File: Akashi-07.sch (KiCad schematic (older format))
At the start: 10 parts, among them U1 Si5351A-B-GT, U2 74HC74, U3 TS5A23157DGSR, U4 AD8032ANZ, X1 SG-615

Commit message: Update the switch symbol
Singal flow is natural now.
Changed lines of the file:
@@
 $EndDescr
-$Comp
-L TS5A23157:TS5A23157DGSR U3
-U 1 1 5F07B13A
-P 8150 1850
-F 0 "U3" H 8950 2337 60  0000 C CNN
-F 1 "TS5A23157DGSR" H 8950 2231 60  0000 C CNN
-F 2 "DGS10" H 8950 2190 60  0001 C CNN
-F 3 "" H 8150 1850 60  0000 C CNN
-	1    8150 1850
-	-1   0    0    -1
-$EndComp
 $Comp
 L Oscillator:Si5351A-B-GT U1
@@
 Text Notes 7050 2950 0    50   ~ 0
 Quadrature Switch
+$Comp
+L TS5A23157:TS5A23157DGSR U3
+U 1 1 5F0916DB
+P 6700 1350
+F 0 "U3" H 7500 1837 60  0000 C CNN
+F 1 "TS5A23157DGSR" H 7500 1731 60  0000 C CNN
+F 2 "DGS10" H 7500 1690 60  0001 C CNN
+F 3 "" H 6700 1350 60  0000 C CNN
+	1    6700 1350
+	1    0    0    -1
+$EndComp
 $EndSCHEMATC

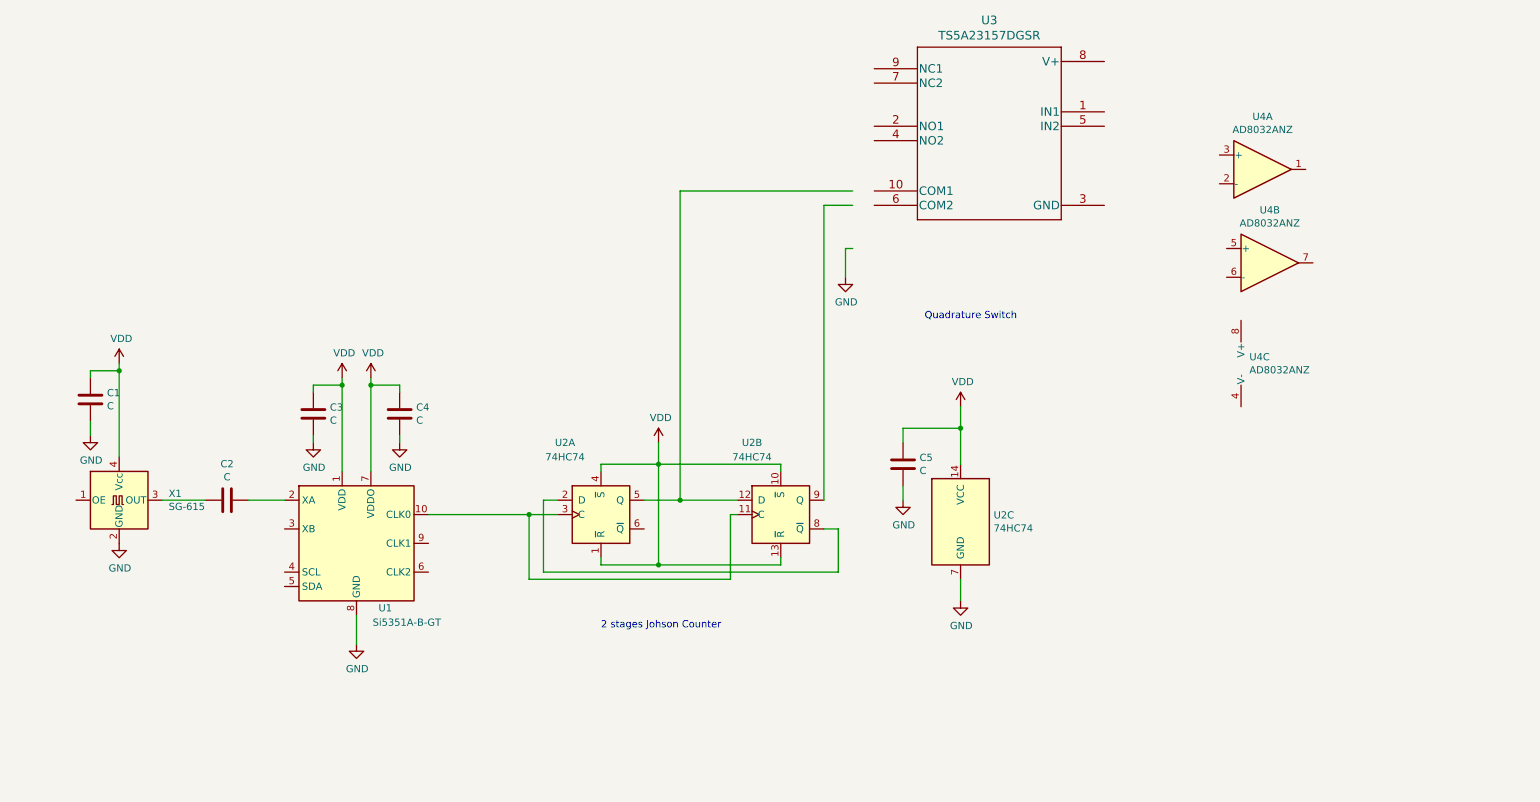
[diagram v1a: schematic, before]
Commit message: Analog part is haf complete
Need to fix the value.
Need to re-annotate
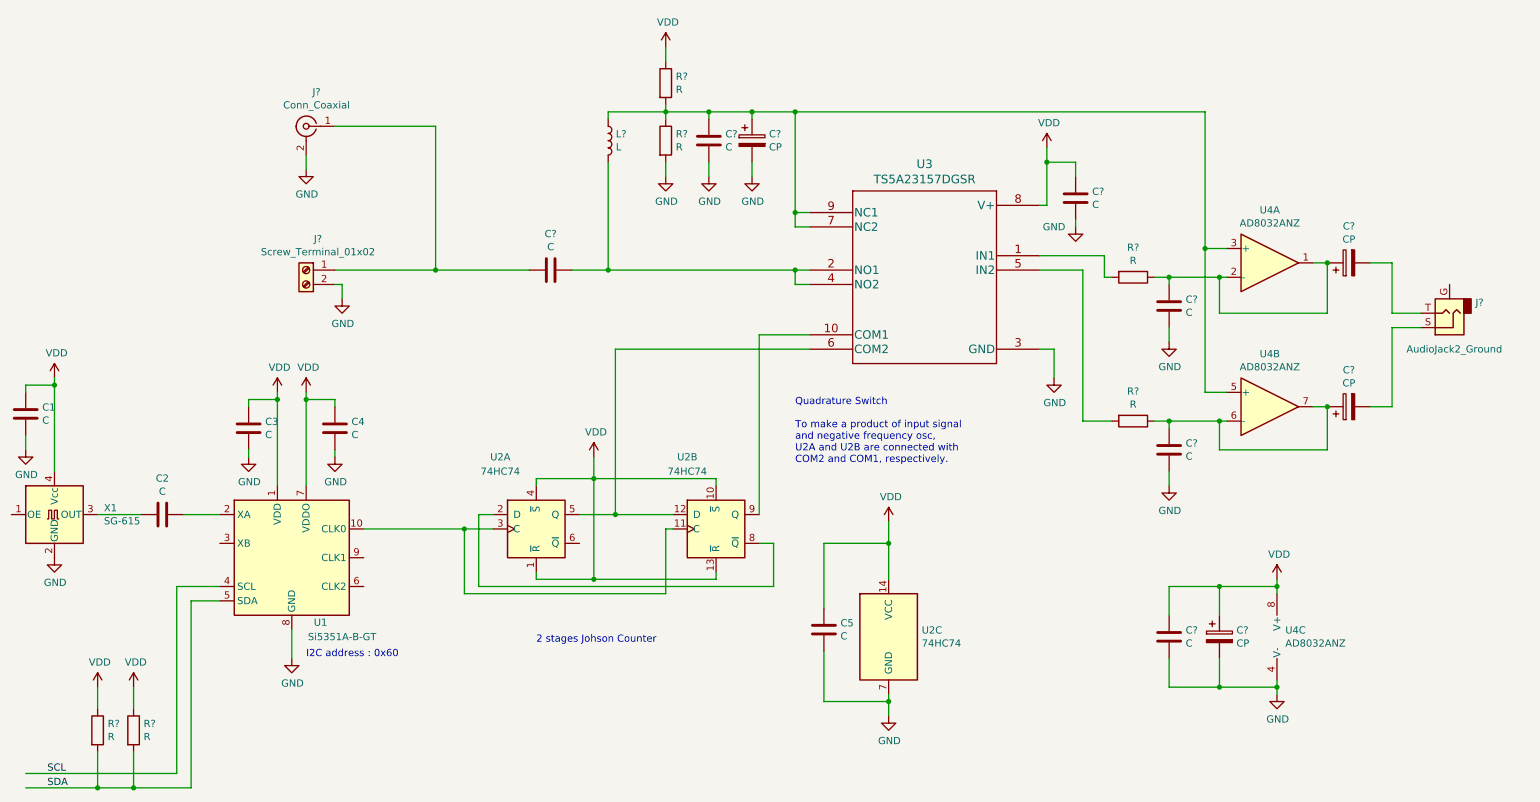
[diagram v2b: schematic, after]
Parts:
- added C? (x6): C, symbol Device:C
- added C? (x4): CP, symbol Device:CP
- added J?: AudioJack2_Ground, symbol Connector:AudioJack2_Ground
- added J?: Conn_Coaxial, symbol Connector:Conn_Coaxial
- added J?: Screw_Terminal_01x02, symbol Connector:Screw_Terminal_01x02
- added L?: L, symbol Device:L
- added R? (x6): R, symbol Device:R
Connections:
- net labels added: SCL, SDA
- wire segments 53 -> 150
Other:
- note added: "I2C address : 0x60"
- note added: "Quadrature Switch\n\nTo make a product of input signal \nand negative frequency osc, \nU2A and U2B are connected with \nCOM2 and COM1, respectively."
- note removed: "Quadrature Switch"
- moved on the sheet: C1, C2, C3, C4, C5, U1, U2A, U2B, U2C, U3, U4A, U4B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

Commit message: Editing the schematics.
Added bypass capacitor values.
Added foot prints.
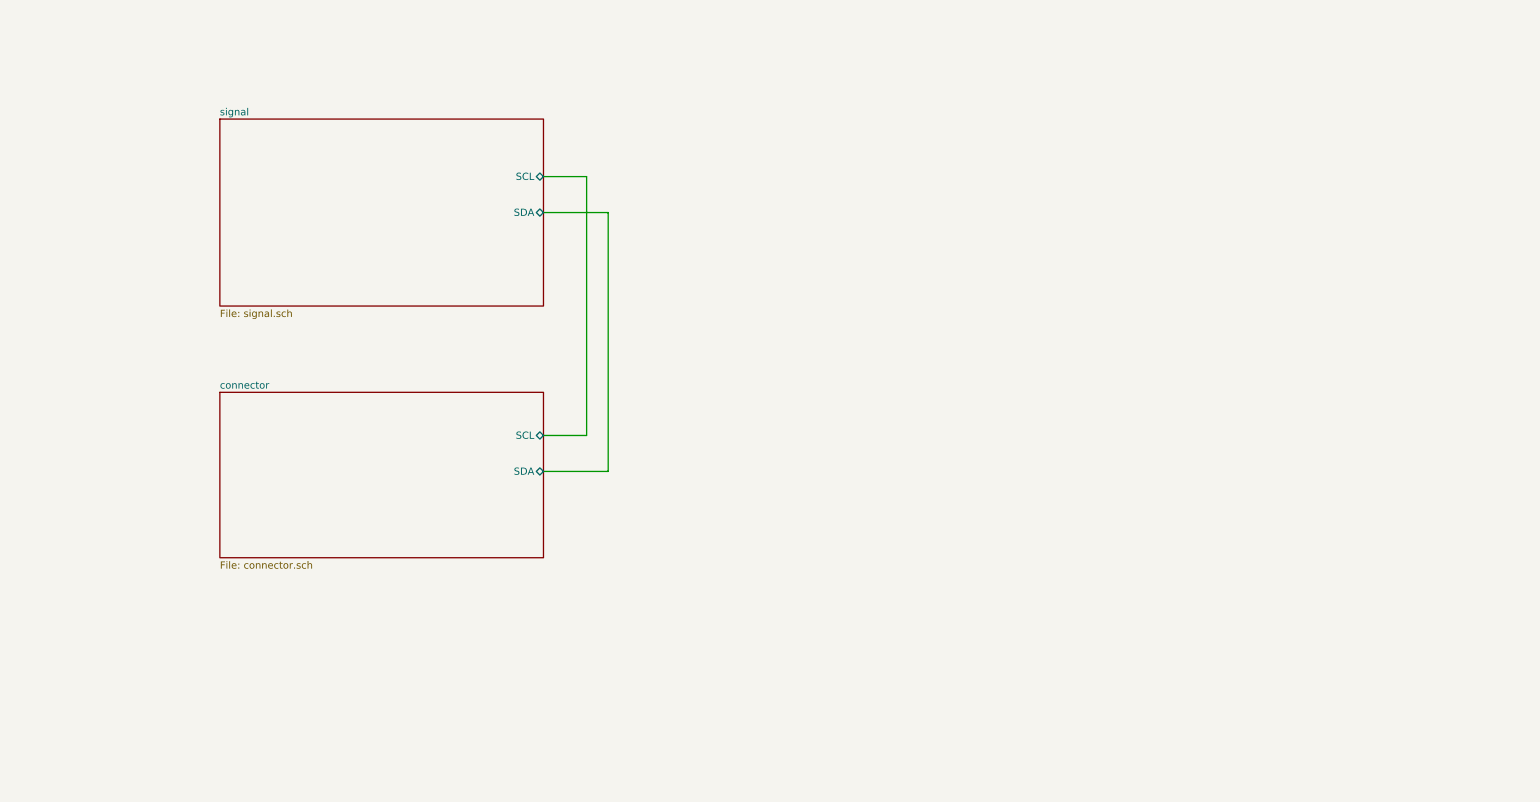
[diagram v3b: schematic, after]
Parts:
- removed C1, C2, C3, C4, C5, C? (x6): C, symbol Device:C
- removed C? (x4): CP, symbol Device:CP
- removed J?: AudioJack2_Ground, symbol Connector:AudioJack2_Ground
- removed J?: Conn_Coaxial, symbol Connector:Conn_Coaxial
- removed J?: Screw_Terminal_01x02, symbol Connector:Screw_Terminal_01x02
- removed L?: L, symbol Device:L
- removed R? (x6): R, symbol Device:R
- removed U1: Si5351A-B-GT, Package_SO:MSOP-10_3x3mm_P0.5mm, symbol Oscillator:Si5351A-B-GT
- removed U2: 74HC74, symbol 74xx:74HC74
- removed U3: TS5A23157DGSR, DGS10, symbol TS5A23157:TS5A23157DGSR
- removed U4: AD8032ANZ, Package_SO:MSOP-8_3x3mm_P0.65mm, symbol Amplifier_Operational:MCP6L02x-xMS
- removed X1: SG-615, Oscillator:Oscillator_SMD_SeikoEpson_SG8002JA-4Pin_14.0x8.7mm, symbol Oscillator:SG-615
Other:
- note removed: "2 stages Johson Counter"
- note removed: "I2C address : 0x60"
- note removed: "Quadrature Switch\n\nTo make a product of input signal \nand negative frequency osc, \nU2A and U2B are connected with \nCOM2 and COM1, respectively."

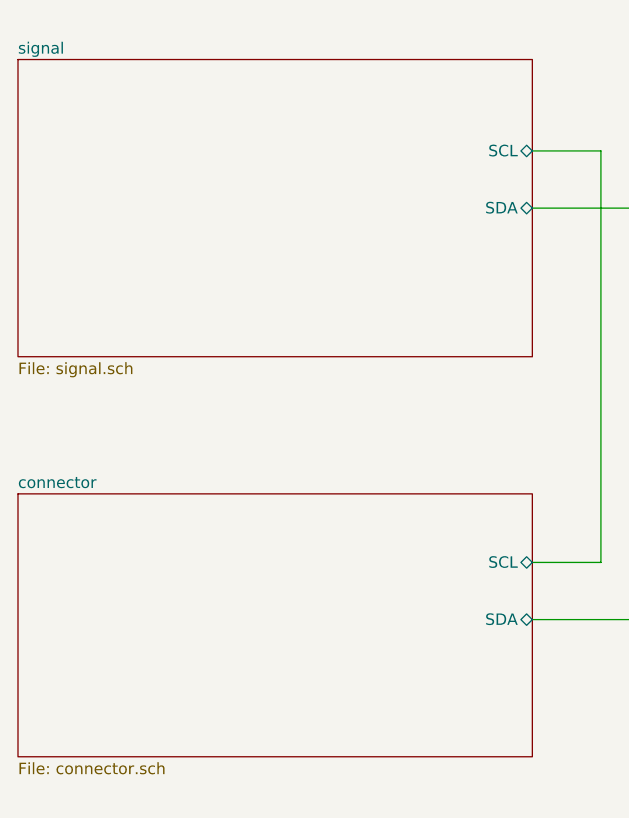
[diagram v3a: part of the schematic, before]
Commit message: Footprint done.
Added footprint of the audio jack.
The documentation link of the each IC is done.
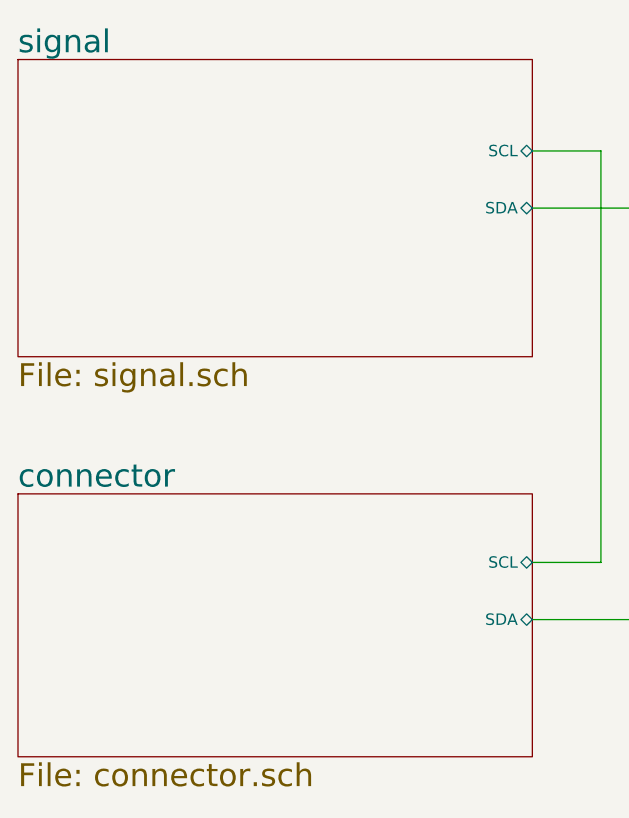
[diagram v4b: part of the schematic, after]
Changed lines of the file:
@@
 S 2150 1550 2250 1300
 U 5F09EE5F
-F0 "signal" 50
-F1 "signal.sch" 50
+F0 "signal" 100
+F1 "signal.sch" 100
 F2 "SCL" B R 4400 1950 50
 F3 "SDA" B R 4400 2200 50
@@
 S 2150 3450 2250 1150
 U 5F0E7241
-F0 "connector" 50
-F1 "connector.sch" 50
+F0 "connector" 100
+F1 "connector.sch" 100
 F2 "SCL" B R 4400 3750 50
 F3 "SDA" B R 4400 4000 50
